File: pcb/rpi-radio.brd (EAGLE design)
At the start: 102.5 x 39.4 mm, 22 parts, among them SW1 EC12E_SW, SW2 EC12E_SW, U1 TDA7052B, U2 TDA7052B

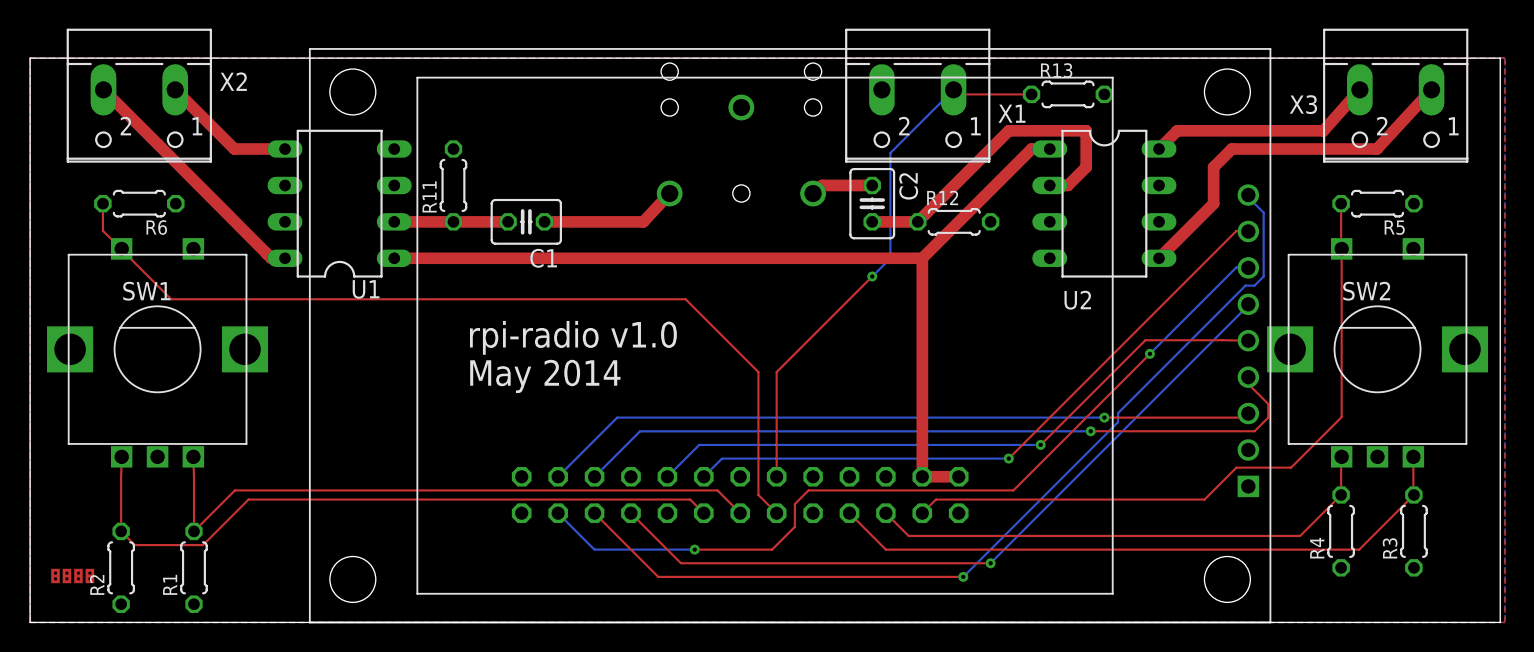
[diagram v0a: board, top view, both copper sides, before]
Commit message: pcb: add attiny2313, because rpi is not able to decode the rotary encoder and use thicker traces
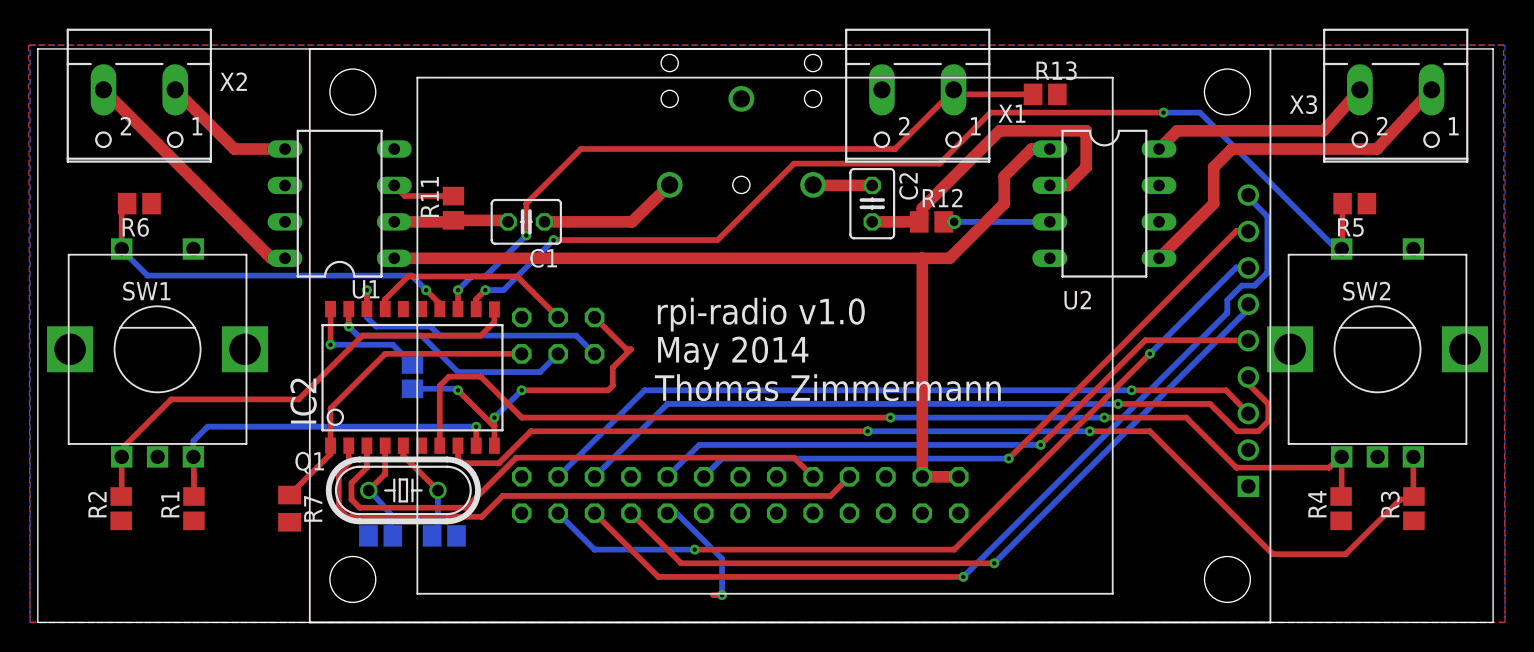
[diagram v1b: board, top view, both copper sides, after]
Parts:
- removed U$3: (no value), Platinensammler:LP_NUMBER_TOP
- added C5: 100n, resistor:C0805
- added C6, C7: 22p, resistor:C0805
- added IC2: AT90S2313S, atmel:SO20L
- added Q1: (no value), crystal:HC49/S
- added R7: 10k, resistor:M0805
- added SV1: (no value), con-ml:ML6
- R1, R11, R12, R13, R2, R3, R4, R5, R6: device resistor:0204/5 -> resistor:R0805
- moved R1 4.13 mm to (12.7, 35.9)
- moved R2 4.13 mm to (7.62, 35.9)
- moved R5 1.59 mm to (93.7, 57.1)
- moved R11 1.59 mm to (30.8, 56.8)
- moved R3 1.59 mm to (97.8, 35.9)
- moved R4 1.59 mm to (92.7, 35.9)
- moved R12 1.59 mm to (64.1, 55.9)
- moved R13 1.59 mm to (72.1, 64.8)
- moved U$5 0.60 mm to (55.9, 67.0)
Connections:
- new net BUT_L: IC2.14, R6.2, SW1.D
- new net BUT_M: IC2.13, R13.1, X1.1
- new net BUT_R: IC2.12, R5.2, SW2.D
- new net ENC_L_A: IC2.11, R2.2, SW1.A
- new net ENC_L_B: IC2.9, R1.2, SW1.B
- new net ENC_R_A: IC2.8, R3.2, SW2.B
- new net ENC_R_B: IC2.7, R4.2, SW2.A
- new net MISO_ISP: IC2.18, SV1.1
- new net MOSI_ISP: IC2.17, SV1.4
- new net N$10: C6.2, IC2.4, Q1.1
- new net N$13: IC2.2, RPI.8
- new net N$14: IC2.3, RPI.10
- new net N$15: C7.2, IC2.5, Q1.2
- new net RESET_ISP: IC2.1, R7.1, SV1.5
- new net SCK_ISP: IC2.19, SV1.3
- net +3V3: now also C5.2, IC2.10, R7.2, SV1.2
- net GND: now also C5.1, C6.1, C7.1, IC2.20, SV1.6
- net GPIO17: no longer R6.2, SW1.D
- net GPIO18: no longer R13.1, X1.1
- net GPIO2: no longer R5.2, SW2.D
- net GPIO22: no longer R2.2, SW1.A
- net GPIO27: no longer R1.2, SW1.B
- net GPIO3: no longer R4.2, SW2.A
- net GPIO4: no longer R3.2, SW2.B
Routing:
- net ENC_R_A: track 0.00 -> 76.6 mm, vias 0 -> 2
- net BUT_R: track 0.00 -> 73.7 mm, vias 0 -> 3
- net ENC_R_B: track 0.00 -> 73.1 mm, vias 0 -> 2
- net GPIO17: track 62.1 -> 0.00 mm
- net BUT_M: track 0.00 -> 48.7 mm, vias 0 -> 2
- net GPIO22: track 47.9 -> 0.00 mm
- net GPIO2: track 47.0 -> 0.00 mm
- net GPIO27: track 45.1 -> 0.00 mm
- net GPIO4: track 44.7 -> 0.00 mm
- net N$13: track 0.00 -> 41.7 mm
- net N$14: track 0.00 -> 38.6 mm
- net GPIO18: track 37.7 -> 0.00 mm, vias 1 -> 0
- net GPIO3: track 36.3 -> 0.00 mm
- net ENC_L_A: track 0.00 -> 33.9 mm
- net +3V3: track 0.00 -> 32.8 mm, vias 0 -> 4
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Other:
- board size 102.5 x 39.4 mm -> 101.5 x 40 mm
- board text added: "rpi-radio v1.0 May 2014 Thomas Zimmermann"
- board text removed: "rpi-radio v1.0 May 2014"

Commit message: Update to version v2 of the pcb. the integrated amplifier did not work properly
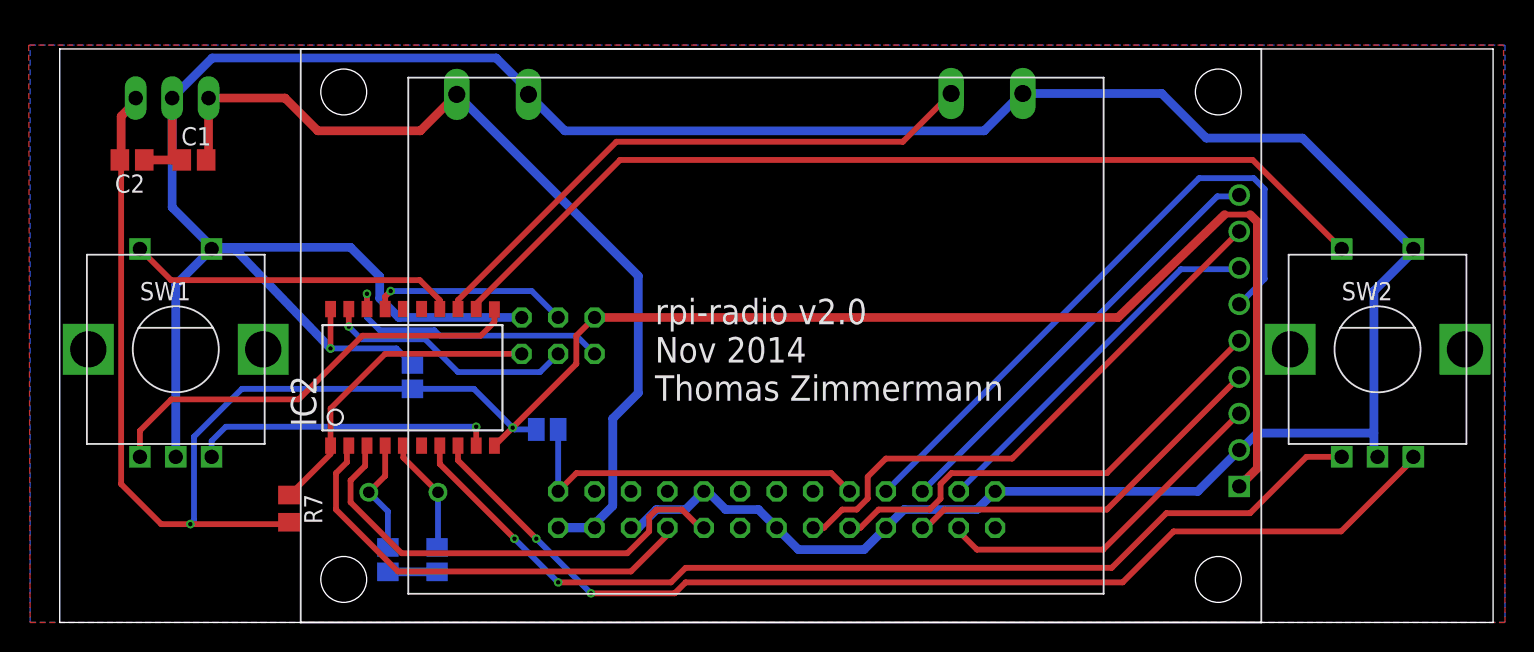
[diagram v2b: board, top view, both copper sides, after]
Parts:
- removed R1, R13, R2, R3, R4, R5, R6: 10k, resistor:R0805
- removed R11, R12: 5k, resistor:R0805
- removed U$5: JACK3.5, rpi-radio:JACK3.5
- removed U1, U2: TDA7052B, tda7052b:DIL08
- removed X3: (no value), con-wago-500:W237-102
- added IC1: (no value), v-reg:78XXS
- added SJ1: (no value), jumper:SJ
- C1, C2: value 470u -> 100n; device resistor:C025-030X050 -> resistor:C0805
- SW1, SW2: device switch-alps:ALPS_EC12E_SW -> rpi-radio:ALPS_EC12E_SW
- moved C2 51.7 mm to (8.38, 60.2), turned to 180 degrees
- moved X2 24.6 mm to (33.5, 63.5), flipped to the bottom
- moved C1 23.6 mm to (12.7, 60.2), turned to 0 degrees
- moved X1 4.83 mm to (68.0, 63.6), flipped to the bottom
- moved RPI 2.74 mm to (53.3, 35.8), turned to 180 degrees
- moved C7 1.73 mm to (29.7, 32.3), turned to 90 degrees
- moved C6 1.73 mm to (26.2, 32.3), turned to 90 degrees
- moved SW1 1.27 mm to (11.4, 47.0)
- moved U$4 0.64 mm to (17.1, 27.9)
- moved Q1 0.13 mm to (27.3, 37.0), flipped to the bottom, turned to 180 degrees
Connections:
- removed net N$1: C2.2, R12.1, U2.2
- removed net N$2: C1.2, R11.1, U1.2
- removed net N$3: C1.1, U$5.E
- removed net N$4: U1.5, X2.1
- removed net N$5: U1.8, X2.2
- removed net N$6: U2.5, X3.1
- removed net N$7: U2.8, X3.2
- removed net N$8: C2.1, U$5.D
- new net VCC: RPI.1, RPI.17, SJ1.1
- net +3V3: now also C2.2, IC1.OUT, SJ1.2; no longer R1.1, R13.2, R2.1, R3.1, R4.1, R5.1, R6.1, RPI.1, RPI.17, U1.4, U2.4
- net +5V: now also C1.2, IC1.IN, X2.1; no longer U1.1, U2.1
- net BUT_L: no longer R6.2
- net BUT_M: no longer R13.1
- net BUT_R: no longer R5.2
- net ENC_L_A: no longer R2.2
- net ENC_L_B: no longer R1.2
- net ENC_R_A: no longer R3.2
- net ENC_R_B: no longer R4.2
- net GND: now also C1.1, C2.1, IC1.GND, X2.2; no longer R11.2, R12.2, U$5.C, U1.3, U1.6, U2.3, U2.6
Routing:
- net GND: track 20.6 -> 251.6 mm, vias 2 -> 1
- net +3V3: track 32.8 -> 153.2 mm, vias 4 -> 2
- net MISO: track 64.0 -> 30.7 mm, vias 1 -> 0
- net SCK: track 57.3 -> 26.0 mm, vias 2 -> 0
- net RESET: track 53.8 -> 26.5 mm, vias 1 -> 0
- net CS: track 51.3 -> 24.3 mm, vias 1 -> 0
- net VCC: track 0.00 -> 25.7 mm
- net N$6: track 25.5 -> 0.00 mm
- net N$1: track 23.7 -> 0.00 mm
- net N$5: track 17.5 -> 0.00 mm
- net N$7: track 15.8 -> 0.00 mm
- net D/C: track 44.5 -> 33.2 mm, vias 1 -> 0
- net N$13: track 41.7 -> 31.3 mm
- net N$3: track 9.78 -> 0.00 mm
- net N$4: track 9.37 -> 0.00 mm
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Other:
- board size 101.5 x 40 mm -> 100 x 40 mm
- board text added: "+"
- board text added: "-"
- board text added: "Power"
- board text added: "rpi-radio v2.0 Nov 2014 Thomas Zimmermann"
- board text removed: "rpi-radio v1.0 May 2014 Thomas Zimmermann"

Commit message: Fix wrong polarity of attiny
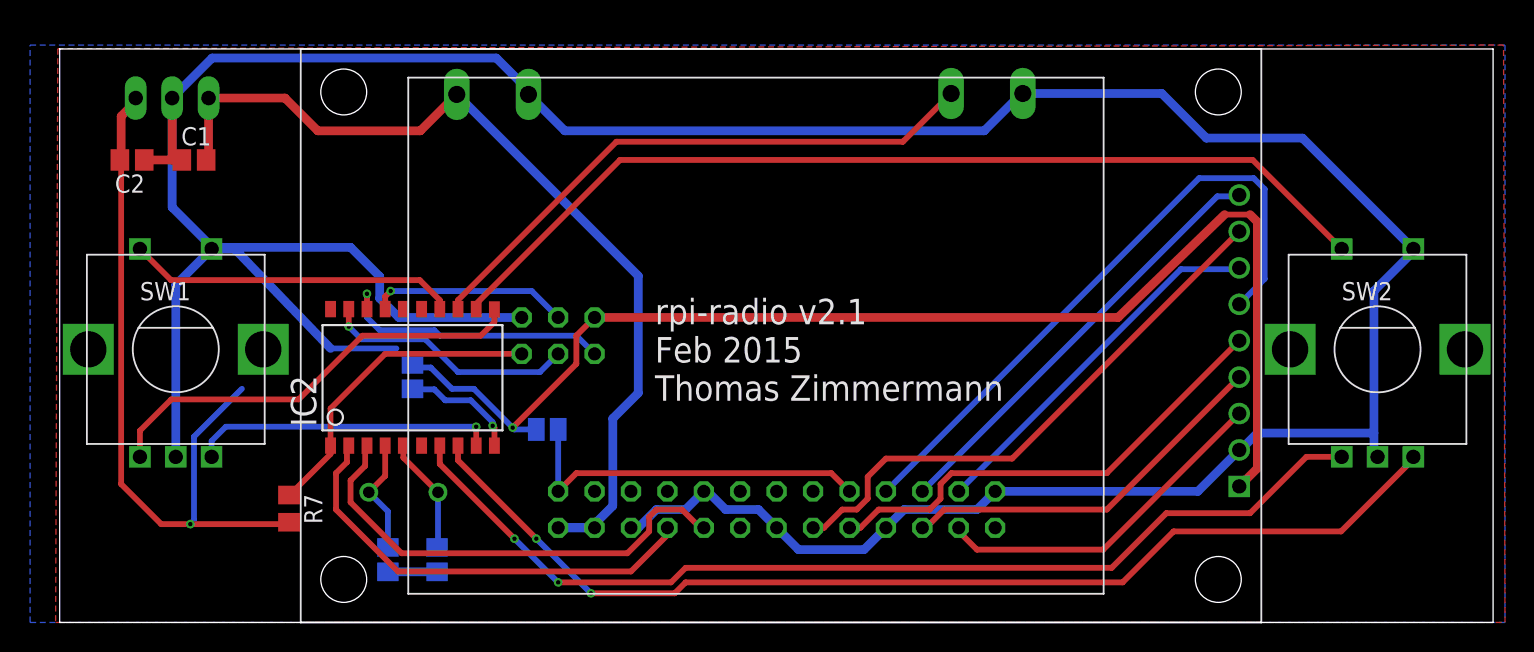
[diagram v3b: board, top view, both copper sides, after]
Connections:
- net +3V3: now also C5.1, IC2.20; no longer C5.2, IC2.10
- net GND: now also C5.2, IC2.10; no longer C5.1, IC2.20
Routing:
- net +3V3: track 153.2 -> 140.2 mm
- net GND: track 251.6 -> 255.5 mm
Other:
- board text added: "rpi-radio v2.1 Feb 2015 Thomas Zimmermann"
- board text removed: "rpi-radio v2.0 Nov 2014 Thomas Zimmermann"
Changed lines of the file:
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@@
 <?xml version="1.0" encoding="utf-8"?>
 <!DOCTYPE eagle SYSTEM "eagle.dtd">
-<eagle version="6.6.0">
+<eagle version="7.2.0">
 <drawing>
 <settings>
@@
 <wire x1="103.31" y1="67.94" x2="3.334" y2="67.94" width="0" layer="20"/>
 <wire x1="3.334" y1="67.94" x2="3.334" y2="27.94" width="0" layer="20"/>
-<text x="44.855" y="43.4025" size="1.778" layer="25" font="vector">rpi-radio v2.0
-Nov 2014
+<text x="44.855" y="43.4025" size="1.778" layer="25" font="vector">rpi-radio v2.1
+Feb 2015
 Thomas Zimmermann</text>
 <dimension x1="1.27" y1="67.94" x2="1.27" y2="27.94" x3="-2.54" y3="47.94" textsize="1.778" layer="51"/>
@@
 <pass name="Default">
 <param name="RoutingGrid" value="50mil"/>
+<param name="AutoGrid" value="1"/>
+<param name="Efforts" value="0"/>
+<param name="TopRouterVariant" value="1"/>
 <param name="tpViaShape" value="round"/>
 <param name="PrefDir.1" value="*"/>
@@
 <contactref element="C7" pad="1"/>
 <contactref element="SV1" pad="6"/>
-<contactref element="C5" pad="1"/>
-<contactref element="IC2" pad="20"/>
-<wire x1="22.225" y1="49.7967" x2="22.225" y2="47.0535" width="0.4" layer="1"/>
-<via x="22.225" y="47.0535" extent="1-16" drill="0.3048"/>
 <wire x1="22.225" y1="47.0535" x2="26.8215" y2="47.0535" width="0.4" layer="16"/>
-<wire x1="26.8215" y1="47.0535" x2="27.94" y2="45.935" width="0.4" layer="16"/>
 <contactref element="IC1" pad="GND"/>
 <contactref element="C1" pad="1"/>
@@
 <wire x1="38.568" y1="62.23" x2="36.028" y2="64.77" width="0.6096" layer="16"/>
 <wire x1="13.97" y1="67.31" x2="33.782" y2="67.31" width="0.6096" layer="16"/>
+<contactref element="C5" pad="2"/>
+<contactref element="IC2" pad="10"/>
+<wire x1="33.655" y1="40.2717" x2="33.655" y2="41.529" width="0.4064" layer="1"/>
+<wire x1="33.655" y1="41.529" x2="33.528" y2="41.656" width="0.4064" layer="1"/>
+<via x="33.528" y="41.656" extent="1-16" drill="0.3048"/>
+<wire x1="33.528" y1="41.656" x2="33.528" y2="41.91" width="0.4064" layer="16"/>
+<wire x1="33.528" y1="41.91" x2="32.004" y2="43.434" width="0.4064" layer="16"/>
+<wire x1="32.004" y1="43.434" x2="30.226" y2="43.434" width="0.4064" layer="16"/>
+<wire x1="30.226" y1="43.434" x2="29.464" y2="44.196" width="0.4064" layer="16"/>
+<wire x1="29.464" y1="44.196" x2="27.979" y2="44.196" width="0.4064" layer="16"/>
+<wire x1="27.979" y1="44.196" x2="27.94" y2="44.235" width="0.4064" layer="16"/>
 </signal>
 <signal name="+3V3">
 <polygon width="0.4064" layer="1">
-<vertex x="1.17" y="68.21"/>
-<vertex x="1.27" y="27.94"/>
+<vertex x="3.202" y="67.956"/>
+<vertex x="3.048" y="27.94"/>
 <vertex x="104.14" y="27.94"/>
 <vertex x="104.04" y="68.21"/>
@@
 <contactref element="R7" pad="2"/>
 <contactref element="SV1" pad="2"/>
-<contactref element="IC2" pad="10"/>
-<contactref element="C5" pad="2"/>
 <contactref element="IC1" pad="OUT"/>
 <contactref element="C2" pad="2"/>
 <contactref element="SJ1" pad="2"/>
-<wire x1="33.655" y1="40.2717" x2="33.6677" y2="40.2717" width="0.4064" layer="1"/>
-<wire x1="33.6677" y1="40.2717" x2="34.925" y2="41.529" width="0.4064" layer="1"/>
 <wire x1="34.925" y1="41.529" x2="39.37" y2="45.974" width="0.4064" layer="1"/>
 <wire x1="39.37" y1="45.974" x2="39.37" y2="47.9425" width="0.4064" layer="1"/>
@@
 <wire x1="86.868" y1="55.88" x2="86.868" y2="38.693" width="0.6096" layer="1"/>
 <wire x1="86.868" y1="38.693" x2="85.605" y2="37.43" width="0.6096" layer="1"/>
-<wire x1="27.94" y1="44.235" x2="32.219" y2="44.235" width="0.4064" layer="16"/>
 <wire x1="32.219" y1="44.235" x2="34.925" y2="41.529" width="0.4064" layer="16"/>
 <wire x1="7.62" y1="60.286" x2="7.62" y2="37.592" width="0.4064" layer="1"/>
@@
 <wire x1="12.446" y1="34.798" x2="19.238" y2="34.798" width="0.4064" layer="1"/>
 <wire x1="19.238" y1="34.798" x2="19.3675" y2="34.9275" width="0.4064" layer="1"/>
-<wire x1="27.94" y1="44.235" x2="16.041" y2="44.235" width="0.4064" layer="16"/>
 <wire x1="16.041" y1="44.235" x2="12.7" y2="40.894" width="0.4064" layer="16"/>
 <wire x1="12.7" y1="40.894" x2="12.7" y2="35.052" width="0.4064" layer="16"/>
 <wire x1="12.7" y1="35.052" x2="12.446" y2="34.798" width="0.4064" layer="16"/>
 <via x="12.446" y="34.798" extent="1-16" drill="0.3048"/>
+<contactref element="C5" pad="1"/>
+<contactref element="IC2" pad="20"/>
+<wire x1="32.219" y1="44.235" x2="30.695" y2="44.235" width="0.4064" layer="16"/>
+<wire x1="30.695" y1="44.235" x2="29.21" y2="45.72" width="0.4064" layer="16"/>
+<wire x1="29.21" y1="45.72" x2="28.155" y2="45.72" width="0.4064" layer="16"/>
+<wire x1="28.155" y1="45.72" x2="27.94" y2="45.935" width="0.4064" layer="16"/>
 </signal>
 <signal name="+5V">
